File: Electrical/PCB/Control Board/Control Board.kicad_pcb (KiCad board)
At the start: 2 copper layers, 154 x 175 mm, 90 parts, among them J1 ED2627-ND, J10 6posheader, J11 S7038-ND, J12 ED2989-ND-USB, J13 ED1501-ND, J14 ED2989-ND-USB, J15 ED2580-ND, J16 ED2580-ND, J17 ED2744-ND, J18 ED2744-ND, J19 ED2744-ND, J2 ED2627-ND, J20 ED2744-ND, J21 ED2744-ND, J22 ED2744-ND, J23 ED2744-ND, J24 ED2744-ND, J25 ED2744-ND, J26 ED2744-ND, J3 ED2627-ND, J4 ED2627-ND, J5 ED2627-ND, J6 S9175-ND, J7 S9175-ND, J8 6posheader, J9 S7038-ND, M1 Mounting_Holes, T1 test_point, T10 test_point, T11 test_point, T12 test_point, T13 test_point, T14 test_point, T15 test_point, T16 test_point, T17 test_point, T18 test_point, T19 test_point, T2 test_point, T20 test_point, T21 test_point, T3 test_point, T4 test_point, T5 test_point, T6 test_point, T7 test_point, T8 test_point, T9 test_point, U1 LM358-N, U2 LM358-N, y1 rover_silkscreen

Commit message: Initial PCB corrections
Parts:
- moved C2 13.5 mm to (133.2, -36.9)
- renumbered J16 to J15
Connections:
- J15 pad 1: +BATT -> Net-(D1-Pad1)
- T19 pad 1: Net-(T19-Pad1) -> Net-(C15-Pad2)
- T3 pad 1: Net-(T3-Pad1) -> +BATT
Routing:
- net Net-(J7-Pad16): track 10.5 -> 0.00 mm
- net +5V: track 1316.0 -> 1319.2 mm
- net Net-(D1-Pad1): track 34.7 -> 36.2 mm
- net +BATT: track 20.9 -> 19.4 mm
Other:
- board text added: "OPEN SOURCE ROVER ROBOTIC BREAKOUT BOARD V1.0 REV - F"
- board text removed: "OPEN SOURCE ROVER ROBOTIC BREAKOUT BOARD V1.0 REV - E"

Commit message: Final Rev F
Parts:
- removed the J15 at (130.6, -7.37)
- added J28: ED2580-ND, JPL Robotics:ED2580-ND, F.Cu at (135.8, -7.68)
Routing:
- net Net-(D1-Pad1): track 36.2 -> 34.7 mm
- net +BATT: track 19.4 -> 20.9 mm
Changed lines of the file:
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@@
     (visible_elements 7FFFFFFF)
     (pcbplotparams
-      (layerselection 0x010fc_ffffffff)
+      (layerselection 0x010f0_ffffffff)
       (usegerberextensions true)
       (usegerberattributes false)
@@
       (drillshape 0)
       (scaleselection 1)
-      (outputdirectory "Gerbers/REV E/"))
+      (outputdirectory "Gerbers/REV F/"))
   )
   (net 0 "")
@@
     (add_net "Net-(T14-Pad1)")
   )
+  (module "JPL Robotics:ED2580-ND" (layer F.Cu)
+    (at 135.763 -7.6835 180)
+    (fp_text reference J28 (at -6.35 1.27) (layer F.SilkS)
+      (effects (font (size 1 1) (thickness 0.15)))
+    )
+    (fp_text value ED2580-ND (at 0 -6.35) (layer F.Fab)
+      (effects (font (size 1 1) (thickness 0.15)))
+    )
+    (fp_line (start -3.81 -5.08) (end -3.81 0) (layer F.SilkS) (width 0.15))
+    (fp_line (start 8.89 -5.08) (end -3.81 -5.08) (layer F.SilkS) (width 0.15))
+    (fp_line (start 8.89 5.08) (end 8.89 -5.08) (layer F.SilkS) (width 0.15))
+    (fp_line (start -3.81 5.08) (end 8.89 5.08) (layer F.SilkS) (width 0.15))
+    (fp_line (start -3.81 0) (end -3.81 5.08) (layer F.SilkS) (width 0.15))
+    (pad 2 thru_hole circle (at 5.08 0 180) (size 2.5 2.5) (drill 1.3) (layers *.Cu *.Mask)
+      (net 26 +BATT))
+    (pad 1 thru_hole rect (at 0 0 180) (size 2.5 2.5) (drill 1.3) (layers *.Cu *.Mask)
+      (net 18 GND))
+  )
   (module "JPL Robotics:rover_image" (layer F.Cu)
     (at 64.1858 -135.7503)
@@
       (net 154 "Net-(D1-Pad2)"))
   )
-  (module "JPL Robotics:ED2580-ND" (layer F.Cu)
-    (at 130.556 -7.366)
-    (fp_text reference J15 (at 10.4902 -4.064) (layer F.SilkS)
-      (effects (font (size 1 1) (thickness 0.15)))
-    )
-    (fp_text value ED2580-ND (at 0 -6.35) (layer F.Fab) hide
-      (effects (font (size 1 1) (thickness 0.15)))
-    )
-    (fp_line (start -3.81 -5.08) (end -3.81 0) (layer F.SilkS) (width 0.15))
-    (fp_line (start 8.89 -5.08) (end -3.81 -5.08) (layer F.SilkS) (width 0.15))
-    (fp_line (start 8.89 5.08) (end 8.89 -5.08) (layer F.SilkS) (width 0.15))
-    (fp_line (start -3.81 5.08) (end 8.89 5.08) (layer F.SilkS) (width 0.15))
-    (fp_line (start -3.81 0) (end -3.81 5.08) (layer F.SilkS) (width 0.15))
-    (pad 2 thru_hole circle (at 5.08 0) (size 2.5 2.5) (drill 1.3) (layers *.Cu *.Mask)
-      (net 18 GND))
-    (pad 1 thru_hole rect (at 0 0) (size 2.5 2.5) (drill 1.3) (layers *.Cu *.Mask)
-      (net 155 "Net-(D1-Pad1)"))
-  )
   (module Resistor_THT:R_Axial_DIN0207_L6.3mm_D2.5mm_P7.62mm_Horizontal (layer F.Cu)
     (at 112.014 -166.3065)
@@
   (segment (start 129.832101 -95.999299) (end 130.5941 -95.2373) (width 0.25) (layer B.Cu) (net 18))
   (segment (start 88.8365 -164.8714) (end 91.2114 -164.8714) (width 2) (layer F.Cu) (net 18))
-  (segment (start 135.646234 -7.366) (end 137.414 -7.366) (width 2) (layer F.Cu) (net 18))
+  (segment (start 135.646234 -7.6835) (end 137.414 -7.6835) (width 2) (layer F.Cu) (net 18))
   (segment (start 73.545 -38.1635) (end 72.5805 -39.128) (width 0.25) (layer F.Cu) (net 18))
   (segment (start 74.295 -38.1635) (end 73.545 -38.1635) (width 0.25) (layer F.Cu) (net 18))
@@
   (segment (start 123.2281 -169.8625) (end 128.6764 -169.8625) (width 2) (layer F.Cu) (net 26))
   (segment (start 133.35 -165.1889) (end 135.7249 -165.1889) (width 2) (layer B.Cu) (net 26))
-  (segment (start 130.556 -7.366) (end 129.056 -7.366) (width 2) (layer B.Cu) (net 155))
+  (segment (start 130.556 -7.6835) (end 129.056 -7.6835) (width 2) (layer B.Cu) (net 26))
   (segment (start 65.913 -41.4655) (end 65.913 -49.5935) (width 0.25) (layer B.Cu) (net 27))
   (segment (start 65.913 -49.5935) (end 66.8655 -50.546) (width 0.25) (layer B.Cu) (net 27))

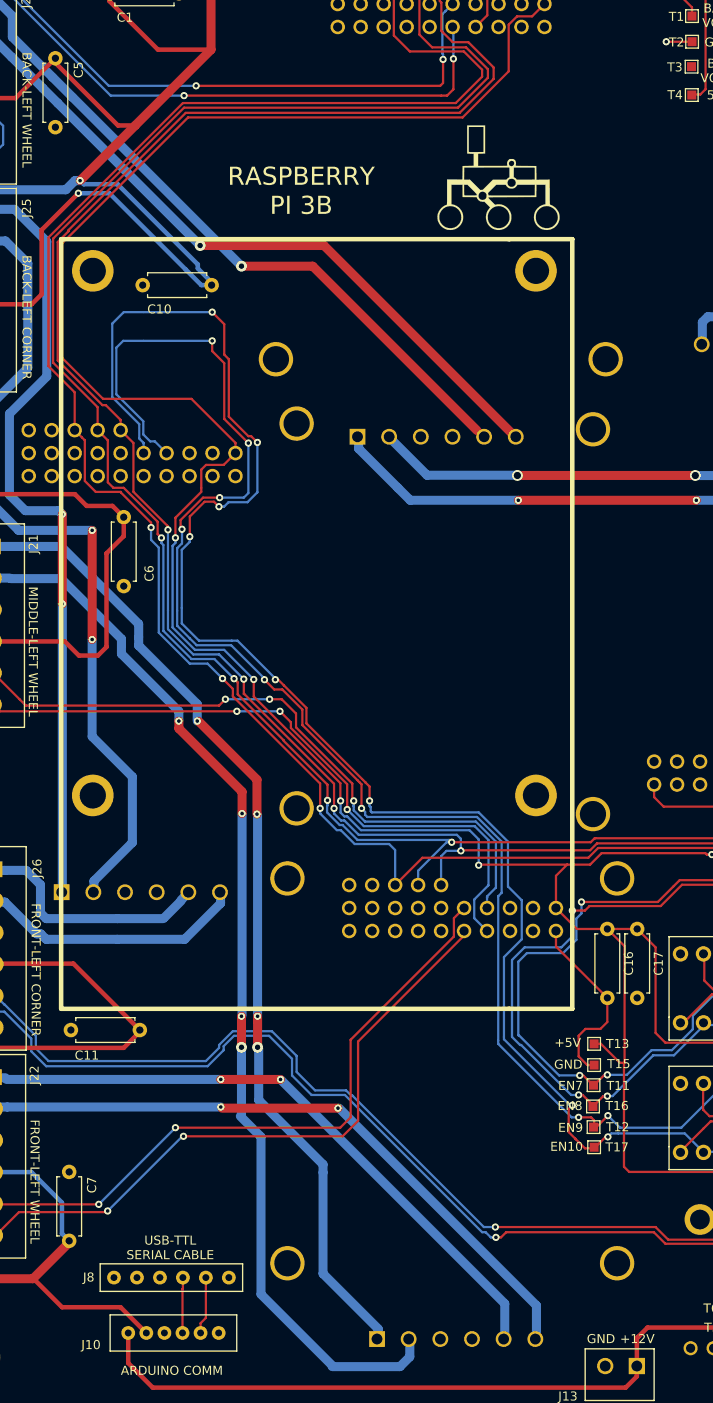
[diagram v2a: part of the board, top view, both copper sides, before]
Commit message: Latest updates - added Gerber files and moved label on 12V connector
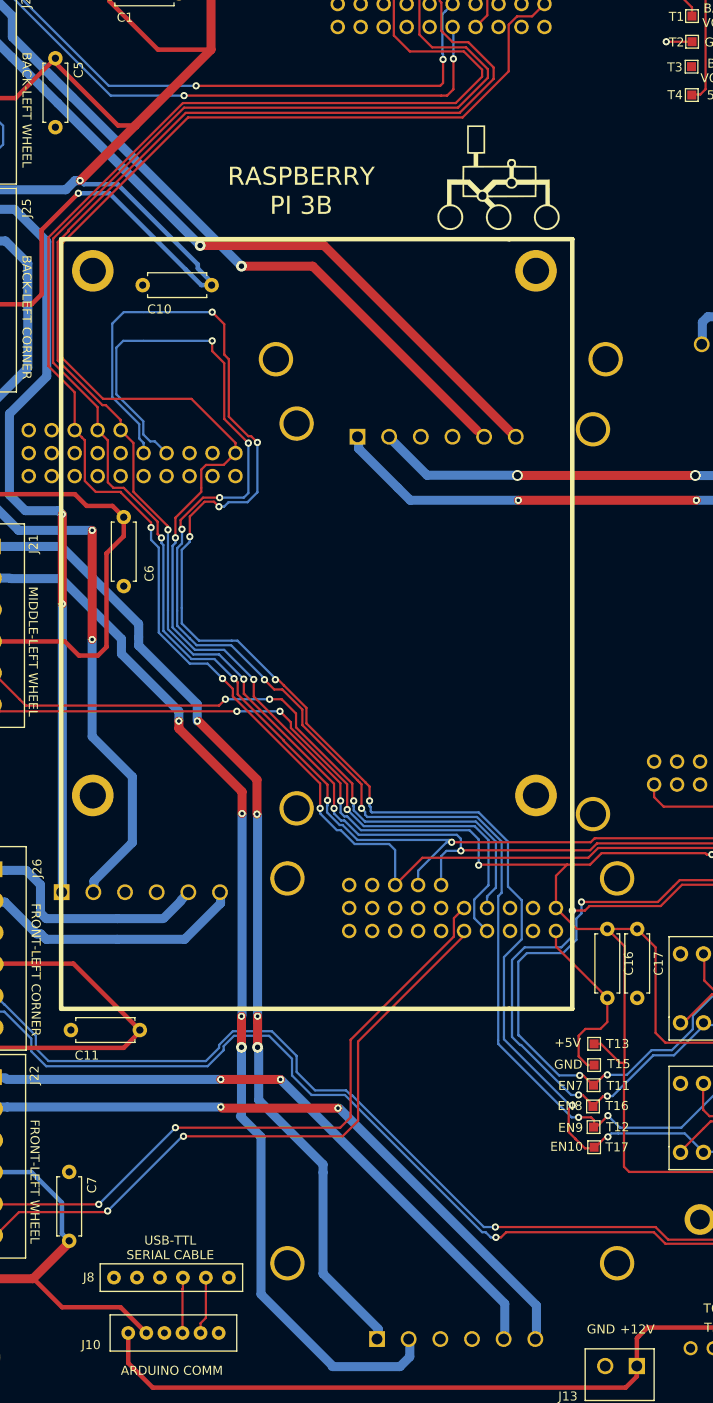
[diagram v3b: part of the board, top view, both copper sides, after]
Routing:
- net +5V: track 1319.2 -> 1318.4 mm
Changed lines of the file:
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@@
     (thickness 1.6)
     (drawings 164)
-    (tracks 1740)
+    (tracks 1739)
     (zones 0)
     (modules 90)
@@
     (effects (font (size 2 2) (thickness 0.3)) (justify mirror))
   )
-  (gr_text GND (at 75.057 -7.8867) (layer F.SilkS)
+  (gr_text GND (at 75.057 -8.9535) (layer F.SilkS)
     (effects (font (size 1 1) (thickness 0.1)))
   )
-  (gr_text +12V (at 79.0702 -7.8867) (layer F.SilkS)
+  (gr_text +12V (at 79.0702 -8.9535) (layer F.SilkS)
     (effects (font (size 1 1) (thickness 0.1)))
   )
@@
   (segment (start 23.5585 -142.0495) (end 17.4625 -135.9535) (width 1) (layer F.Cu) (net 23))
   (segment (start 31.9405 -150.4315) (end 23.5585 -142.0495) (width 1) (layer F.Cu) (net 23))
-  (segment (start 14.732 -148.971) (end 14.732 -149.7965) (width 0.25) (layer F.Cu) (net 23))
   (segment (start 23.5585 -142.0495) (end 21.6535 -142.0495) (width 0.5) (layer F.Cu) (net 23))
   (segment (start 21.6535 -142.0495) (end 14.732 -148.971) (width 0.5) (layer F.Cu) (net 23))

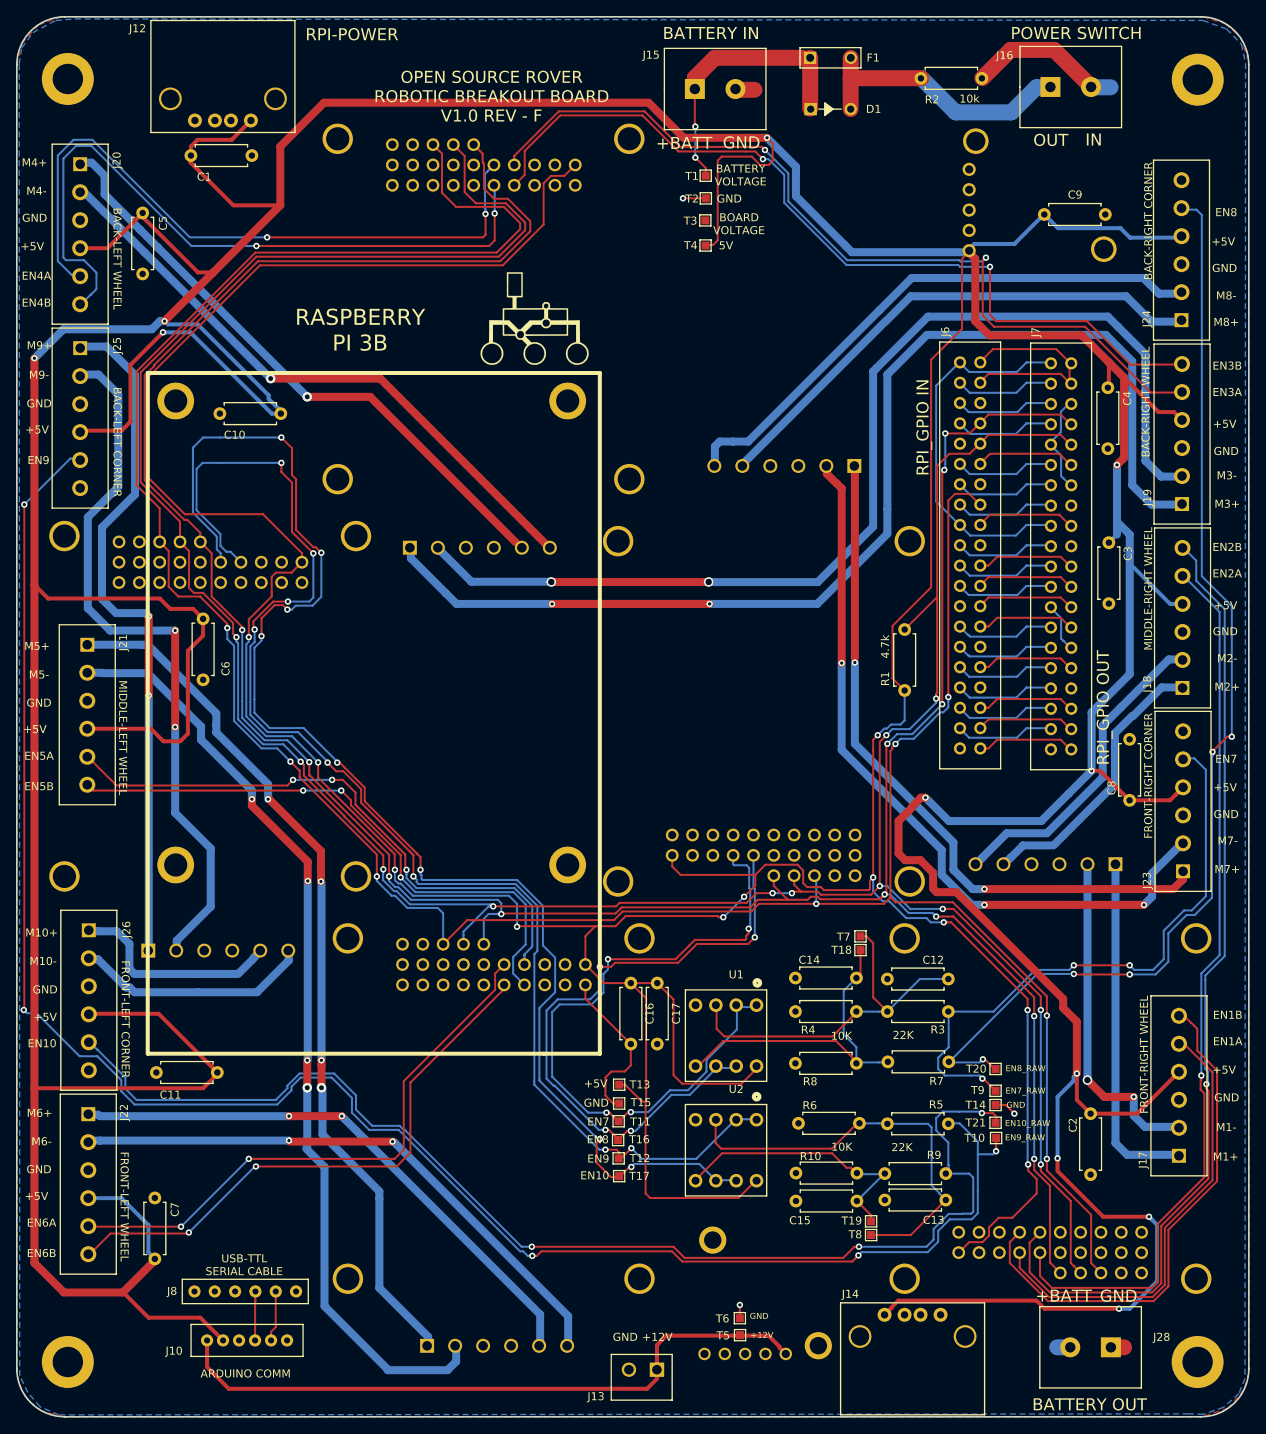
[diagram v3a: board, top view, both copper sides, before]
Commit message: Voltage and ground changes to J6 and J7, eliminate J12 and C1
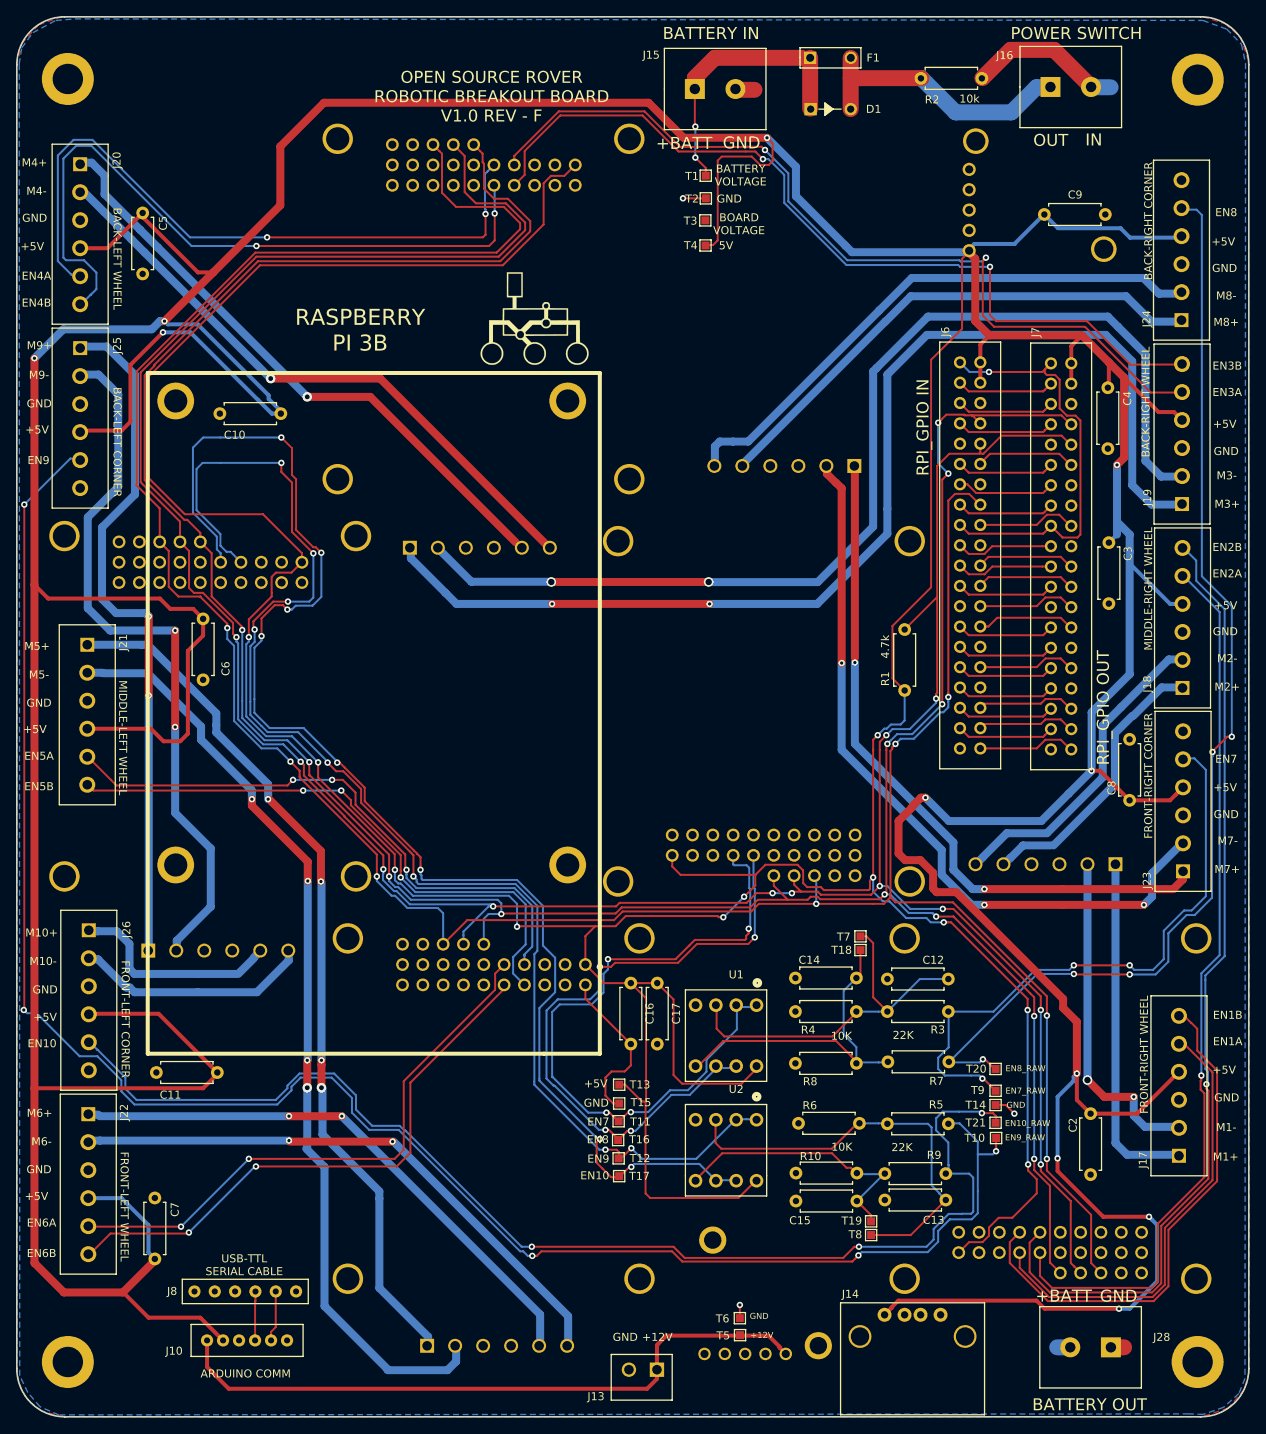
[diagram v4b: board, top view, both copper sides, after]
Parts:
- removed C1: 0.1mF, Resistor_THT:R_Axial_DIN0207_L6.3mm_D2.5mm_P7.62mm_Horizontal
- removed J12: ED2989-ND-USB, JPL Robotics:ED2989-ND USB Conn
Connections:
- J6 pad 14: Net-(J6-Pad14) -> GND
- J6 pad 2: /PI_5V -> +5V
- J6 pad 20: Net-(J6-Pad20) -> GND
- J6 pad 25: Net-(J6-Pad25) -> GND
- J6 pad 30: Net-(J6-Pad30) -> GND
- J6 pad 34: Net-(J6-Pad34) -> GND
- J6 pad 39: Net-(J6-Pad39) -> GND
- J6 pad 4: /PI_5V -> +5V
- J6 pad 6: Net-(J6-Pad6) -> GND
- J6 pad 9: Net-(J6-Pad9) -> GND
- J7 pad 2: /PI_5V -> +5V
- J7 pad 4: /PI_5V -> +5V
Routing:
- net /PI_5V: track 27.2 -> 0.00 mm
- net GND: track 47.7 -> 29.3 mm
- net +5V: track 1318.4 -> 1306.8 mm
- net /3.3V: track 47.3 -> 53.8 mm, vias 0 -> 1
- net /TXD: track 363.0 -> 366.9 mm
- net /RXD: track 368.0 -> 369.2 mm
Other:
- board text removed: "RPI-POWER"
